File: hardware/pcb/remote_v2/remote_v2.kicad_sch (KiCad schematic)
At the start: 26 parts

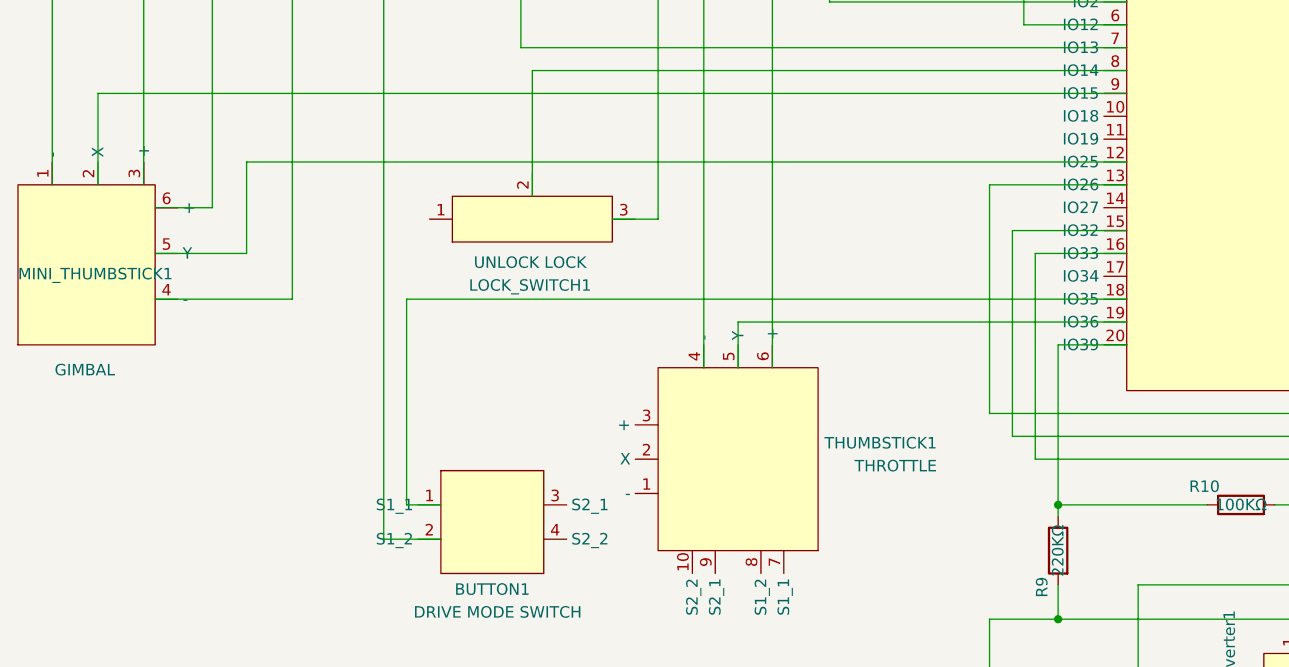
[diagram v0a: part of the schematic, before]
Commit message: remote: Update PCB for remote.
Fix the issue that GPIO 35 does not have internal PULLUP resistor.
So switch the pin with the gimbal thumbstick input Y, instead of the
drive mode button.

Update sensor and tag pcb as well to reflect the changes.
- tag: Use pin 39 for battery measurement and revert the resistor value
  change that's done in the previous commit.
- sensor: Fix a wiring issue.
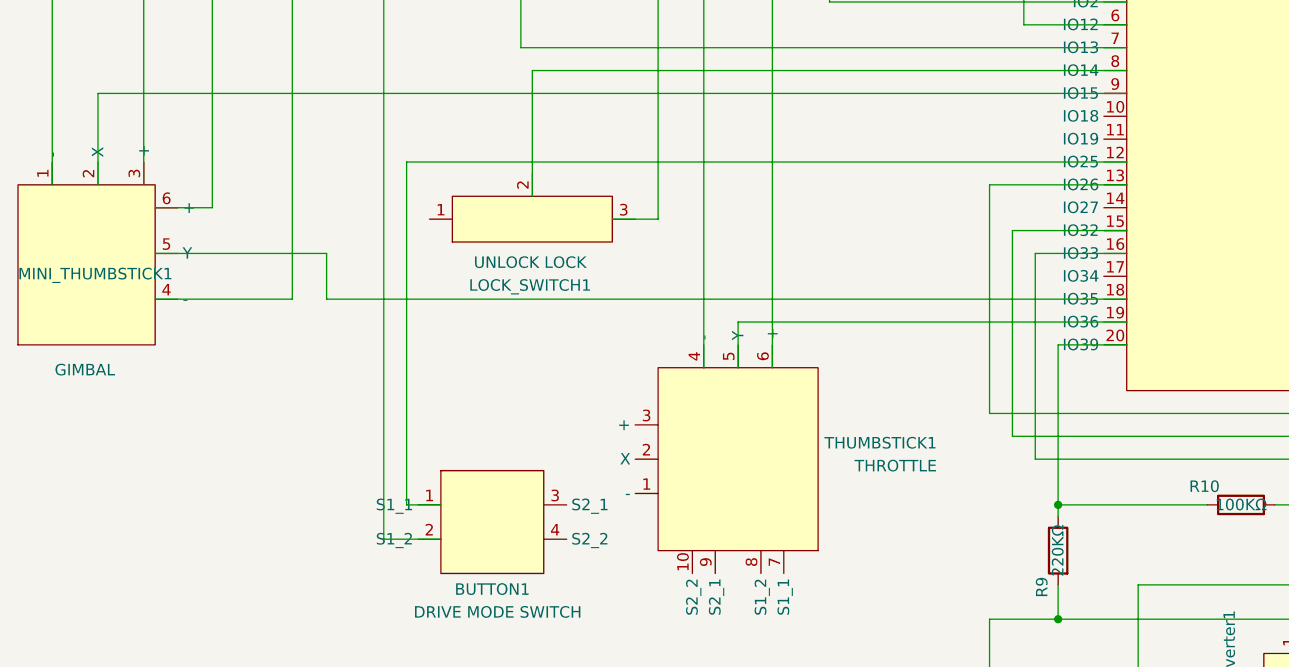
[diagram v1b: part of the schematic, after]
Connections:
- net at MINI_THUMBSTICK1.5 (Y): now also ESP32_UWB1.18 (IO35); no longer ESP32_UWB1.12 (IO25)
- net at BUTTON1.1 (S1_1): now also ESP32_UWB1.12 (IO25); no longer ESP32_UWB1.18 (IO35)
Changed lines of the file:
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@@
-	(wire
-		(pts
-			(xy 138.43 100.33) (xy 40.64 100.33)
-		)
-		(stroke
-			(width 0)
-			(type default)
-		)
-	)
 	(wire
 		(pts
@@
 	(wire
 		(pts
+			(xy 58.42 100.33) (xy 58.42 138.43)
+		)
+		(stroke
+			(width 0)
+			(type default)
+		)
+	)
+	(wire
+		(pts
 			(xy 199.39 82.55) (xy 199.39 99.06)
 		)
@@
 	(wire
 		(pts
-			(xy 40.64 100.33) (xy 40.64 110.49)
-		)
-		(stroke
-			(width 0)
-			(type default)
-		)
-	)
-	(wire
-		(pts
 			(xy 99.06 58.42) (xy 109.22 58.42)
 		)
@@
 	(wire
 		(pts
-			(xy 58.42 115.57) (xy 58.42 138.43)
-		)
-		(stroke
-			(width 0)
-			(type default)
-		)
-	)
-	(wire
-		(pts
 			(xy 213.36 104.14) (xy 195.58 104.14)
 		)
@@
 	(wire
 		(pts
-			(xy 40.64 110.49) (xy 30.48 110.49)
+			(xy 30.48 110.49) (xy 49.53 110.49)
 		)
 		(stroke
@@
 	(wire
 		(pts
-			(xy 138.43 115.57) (xy 58.42 115.57)
-		)
-		(stroke
-			(width 0)
-			(type default)
-		)
-	)
-	(wire
-		(pts
 			(xy 91.44 80.01) (xy 91.44 123.19)
 		)
@@
 	(wire
 		(pts
+			(xy 138.43 115.57) (xy 49.53 115.57)
+		)
+		(stroke
+			(width 0)
+			(type default)
+		)
+	)
+	(wire
+		(pts
 			(xy 195.58 97.79) (xy 180.34 97.79)
 		)
@@
 	(wire
 		(pts
+			(xy 49.53 115.57) (xy 49.53 110.49)
+		)
+		(stroke
+			(width 0)
+			(type default)
+		)
+	)
+	(wire
+		(pts
 			(xy 45.72 80.01) (xy 45.72 115.57)
 		)
 		(stroke
+			(width 0)
+			(type default)
+		)
+	)
+	(wire
+		(pts
+			(xy 138.43 100.33) (xy 58.42 100.33)
+		)
+		(stroke
